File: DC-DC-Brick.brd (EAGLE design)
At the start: 48.5 x 76.2 mm, 20 parts

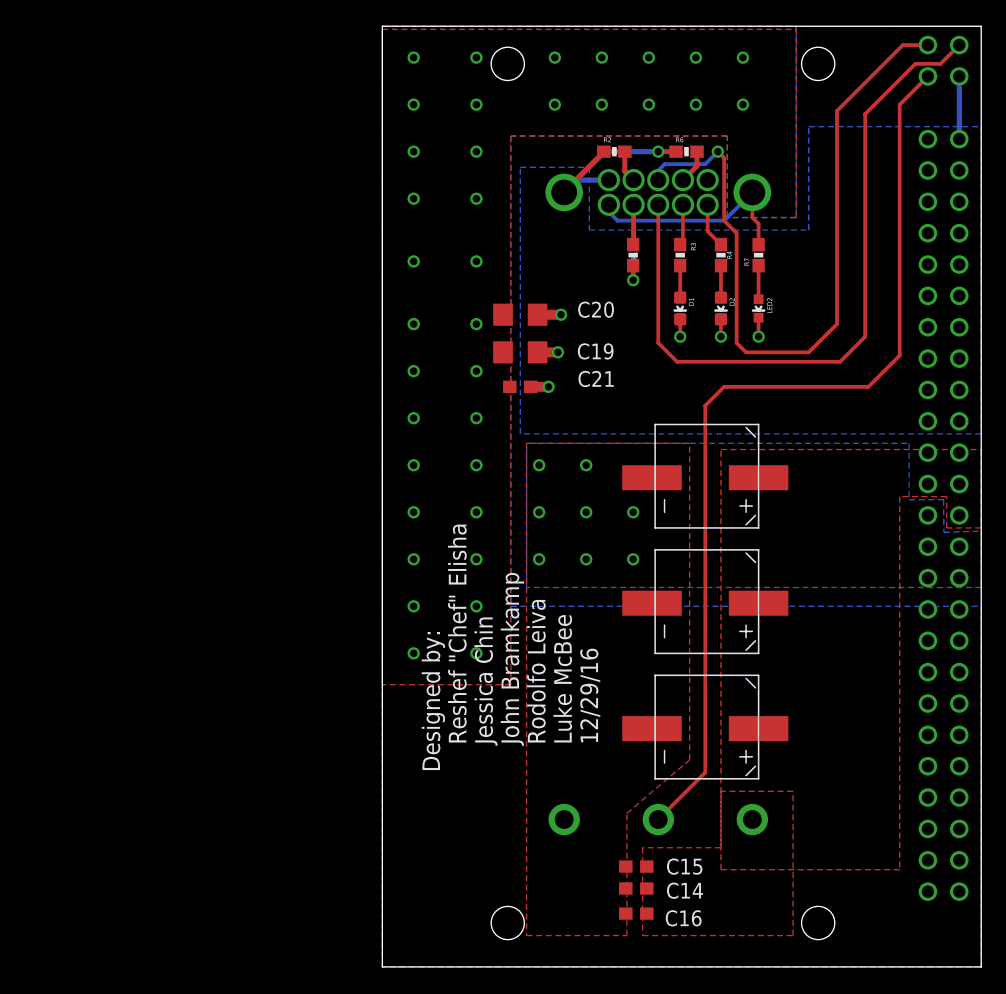
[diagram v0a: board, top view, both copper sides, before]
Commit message: Power brick connectors edited
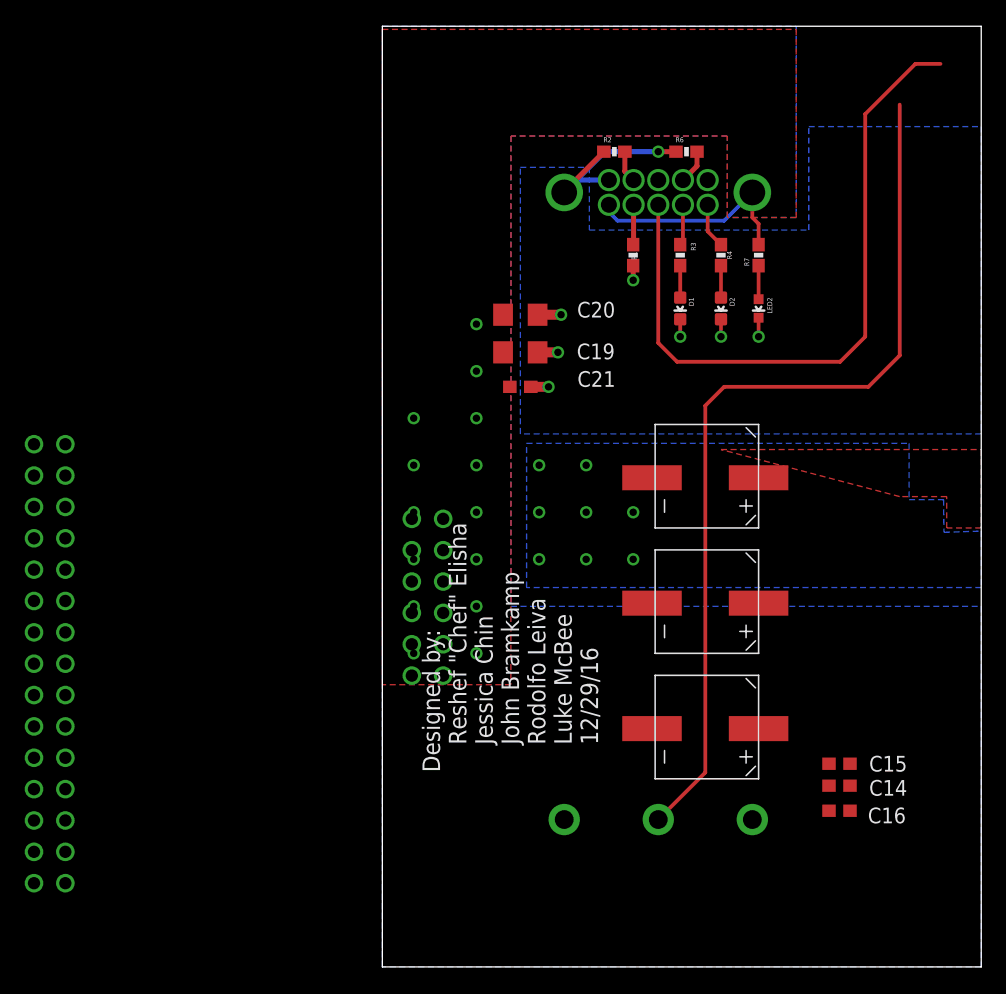
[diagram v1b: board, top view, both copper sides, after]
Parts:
- added U$2: POWER_BRICK_CONNECTORS(2X6), MotherBoardParts2:POWER_BRICK_CONNECTORS(2X6)
- U$3: value POWER-BRICK-CONNECTOR -> POWER_BRICK_CONNECTORS(2X15); device MotherboardParts:POWER-BRICK-CONNECTOR -> MotherBoardParts2:POWER_BRICK_CONNECTORS(2X15)
- moved U$3 74.4 mm to (-26.9, 23.3)
- moved C14 18.4 mm to (37.0, 14.7)
- moved C15 18.4 mm to (37.0, 16.5)
- moved C16 18.4 mm to (37.0, 12.6)
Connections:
- removed net N$10: U$1.10, U$3.P$54
- removed net N$8: U$1.11, U$3.P$53
- removed net V+: C19.1, C20.1, C21.1, R7.2, U$1.16, U$1.6, U$3.P$1, U$3.P$10, U$3.P$11, U$3.P$12, U$3.P$13, U$3.P$14, U$3.P$15, U$3.P$16, U$3.P$17, U$3.P$18, U$3.P$19, U$3.P$2, U$3.P$20, U$3.P$3, U$3.P$4, U$3.P$5, U$3.P$6, U$3.P$7, U$3.P$8, U$3.P$9
- removed net VCC: C14.1, C15.1, C16.1, C22V1.P$3, C22V5.P$3, C22V6.P$3, U$1.1, U$3.P$26, U$3.P$27, U$3.P$28, U$3.P$29, U$3.P$30
- new net +12V: C19.1, C20.1, C21.1, R7.2, U$1.16, U$1.6, U$3.P$1, U$3.P$16, U$3.P$17, U$3.P$18, U$3.P$19, U$3.P$2, U$3.P$20, U$3.P$21, U$3.P$22, U$3.P$3, U$3.P$4, U$3.P$5, U$3.P$6, U$3.P$7
- new net 48V: C14.1, C15.1, C16.1, C22V1.P$3, C22V5.P$3, C22V6.P$3, U$1.1, U$2.P$1, U$2.P$2, U$2.P$7, U$2.P$8
- new net 48V_GND: C14.2, C15.2, C16.2, C22V1.P$1, C22V5.P$1, C22V6.P$1, U$2.P$10, U$2.P$3, U$2.P$4, U$2.P$9
- new net SCL: U$1.10, U$2.P$12
- new net SDA: U$1.11, U$2.P$6
- net GND: now also U$2.P$5, U$3.P$10, U$3.P$11, U$3.P$12, U$3.P$13, U$3.P$14, U$3.P$15, U$3.P$24, U$3.P$25, U$3.P$26, U$3.P$27, U$3.P$28, U$3.P$29, U$3.P$30, U$3.P$9; no longer U$3.P$31, U$3.P$32, U$3.P$33, U$3.P$34, U$3.P$35, U$3.P$36, U$3.P$37, U$3.P$38, U$3.P$39, U$3.P$40, U$3.P$41, U$3.P$42, U$3.P$43, U$3.P$44, U$3.P$45, U$3.P$46, U$3.P$47, U$3.P$48, U$3.P$49, U$3.P$50, U$3.P$52
- net ON/OFF: now also U$2.P$11; no longer U$3.P$51
- net V-: no longer C14.2, C15.2, C16.2, C22V1.P$1, C22V5.P$1, C22V6.P$1, U$3.P$21, U$3.P$22, U$3.P$23, U$3.P$24, U$3.P$25
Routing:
- net N$8: track 58.6 -> 0.00 mm, vias 1 -> 0
- net N$10: track 57.4 -> 0.00 mm
- net SCL: track 0.00 -> 55.2 mm
- net V+: track 17.9 -> 0.00 mm, vias 36 -> 0
- net +12V: track 0.00 -> 17.9 mm, vias 0 -> 14
- net GND: track 34.7 -> 29.6 mm
- net ON/OFF: track 76.1 -> 72.9 mm
- added copper zone on layer 1, net +12V
- added copper zone on layer 16, net +12V
- added copper zone on layer 1, net 48V
- removed copper zone on layer 1, net V+
- removed copper zone on layer 16, net V+
- removed copper zone on layer 1, net V-
- removed copper zone on layer 1, net VCC

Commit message: New power brick board
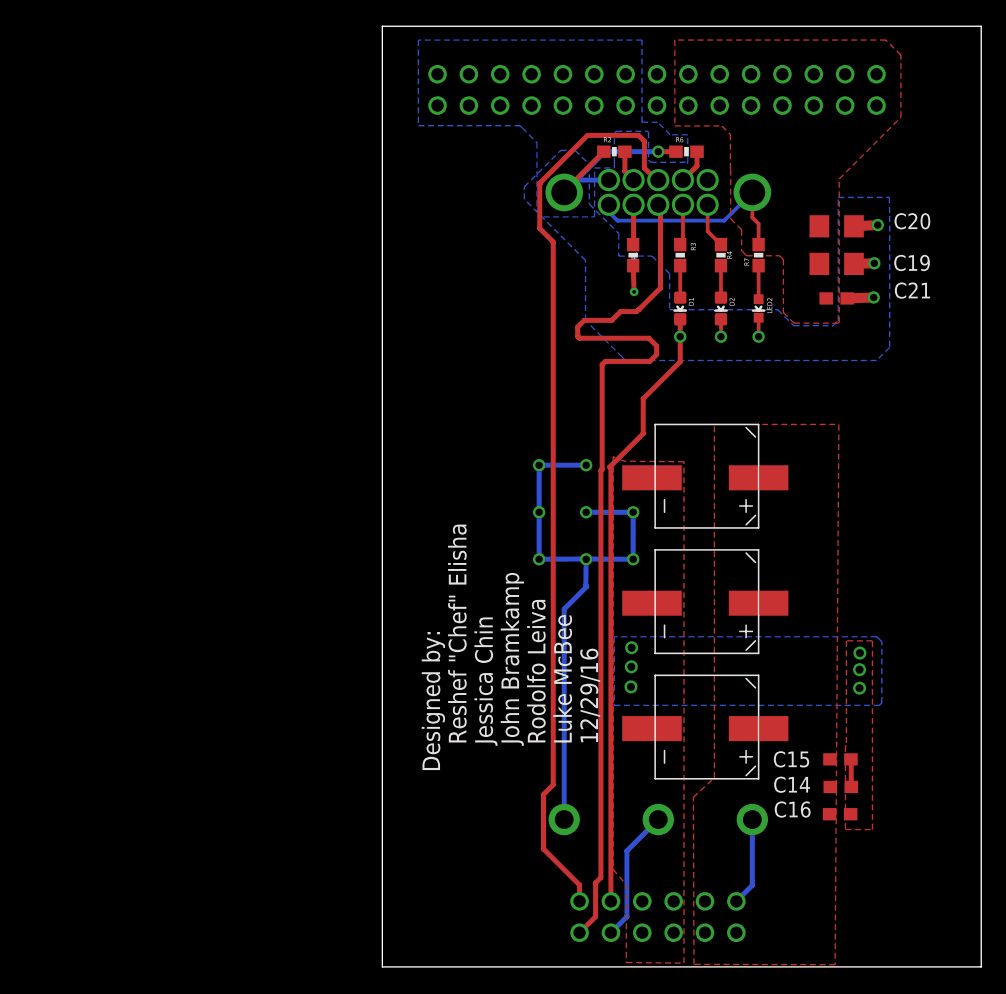
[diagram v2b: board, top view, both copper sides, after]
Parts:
- moved U$3 67.7 mm to (21.0, 71.0), turned to 270 degrees
- moved U$2 31.9 mm to (22.3, 4.04), turned to 270 degrees
- moved C19 26.6 mm to (36.8, 56.9)
- moved C20 26.6 mm to (36.8, 60.0)
- moved C21 26.6 mm to (36.8, 54.2)
- moved C15 0.36 mm to (37.1, 16.8), turned to 0 degrees
- moved C16 0.28 mm to (37.1, 12.4), turned to 0 degrees
- moved C14 0.14 mm to (37.1, 14.6), turned to 0 degrees
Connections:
- net +12V renamed 12V
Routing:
- net SDA: track 0.00 -> 74.1 mm
- net ON/OFF: track 72.9 -> 10.8 mm
- net GND: track 29.6 -> 79.5 mm
- net V-: track 0.00 -> 48.6 mm
- net SCL: track 55.2 -> 74.5 mm
- net 48V: track 0.00 -> 7.17 mm
- net 48V_GND: track 0.00 -> 2.25 mm, vias 0 -> 6
- net 12V: vias 14 -> 0
- added copper zone on layer 1, net 48V_GND
- added copper zone on layer 16, net 48V_GND
- removed copper zone on layer 16, net 12V
- removed copper zone on layer 16, net V-

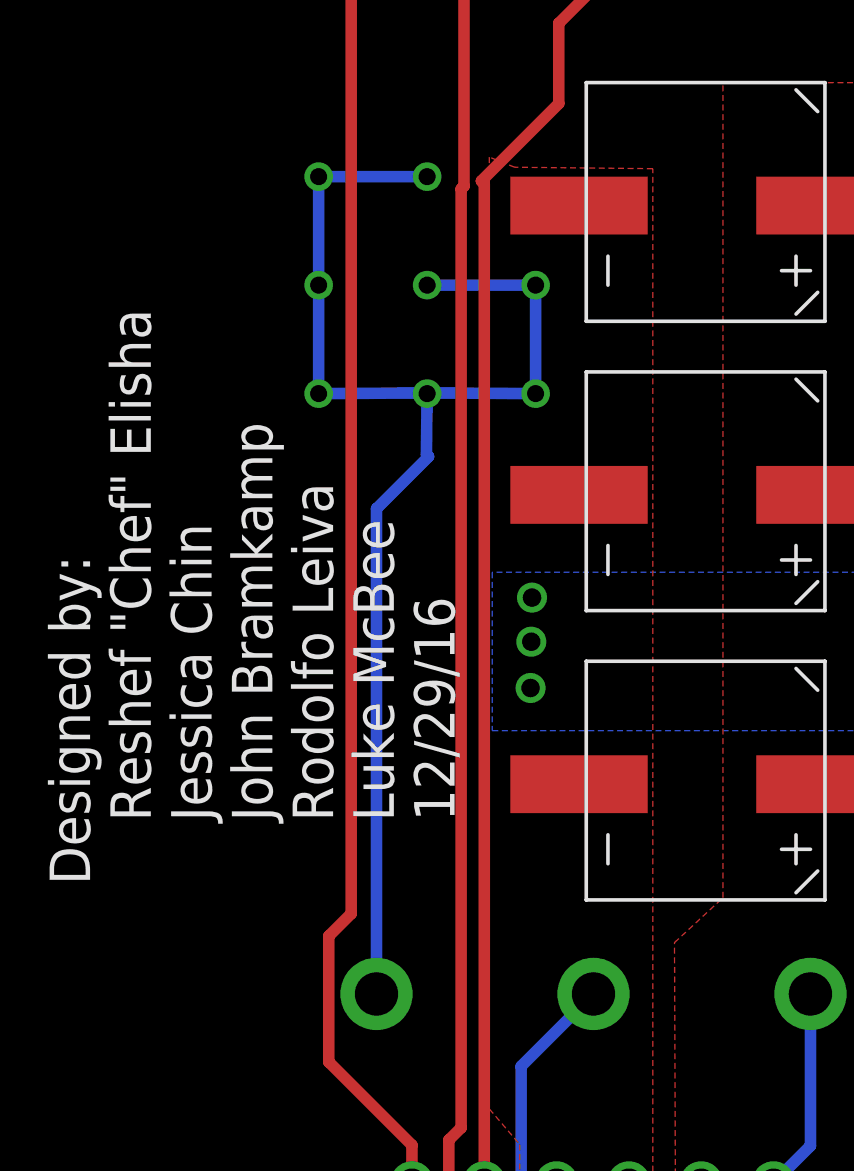
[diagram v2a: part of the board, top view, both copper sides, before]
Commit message: Edit Signal Name
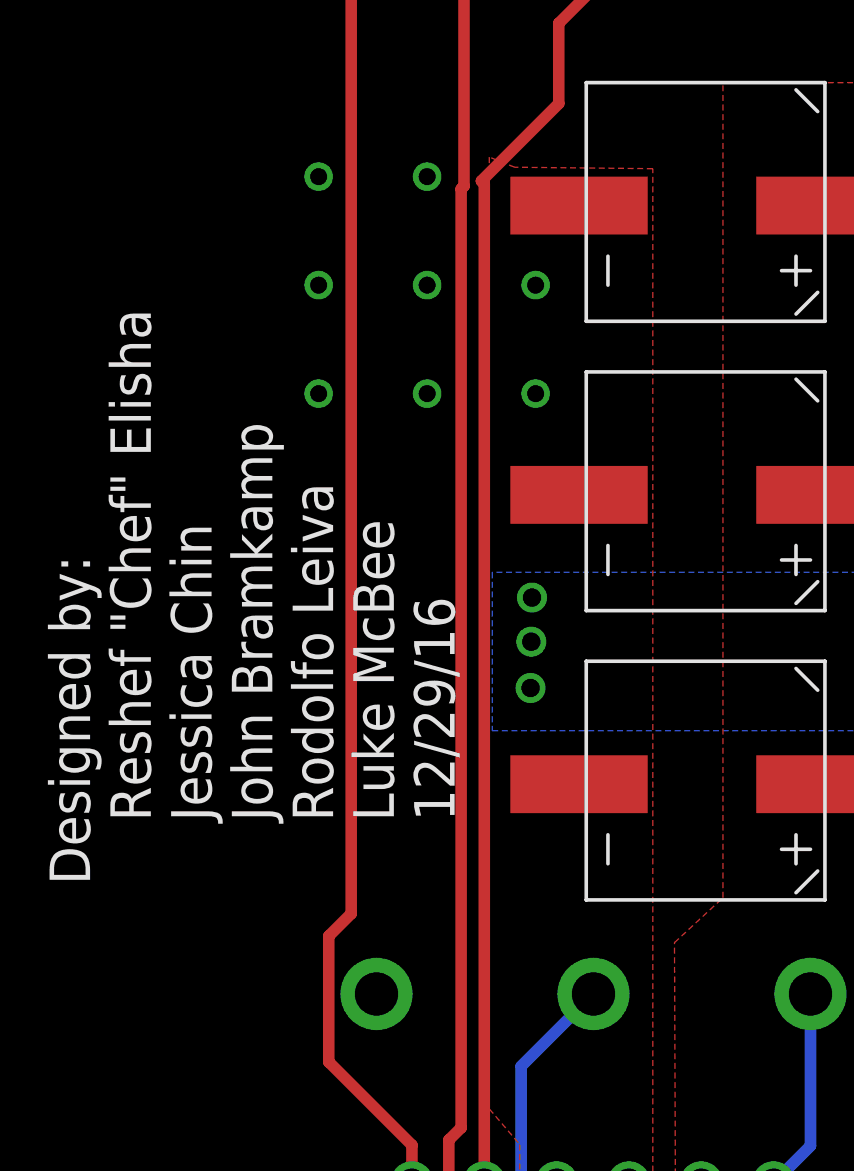
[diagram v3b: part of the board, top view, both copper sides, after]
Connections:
- removed net V-: U$1.4
- net 48V_GND: now also U$1.4
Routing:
- net V-: track 48.6 -> 0.00 mm, vias 8 -> 0
- net 48V_GND: track 2.25 -> 2.27 mm, vias 6 -> 14
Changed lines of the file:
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@@
 <?xml version="1.0" encoding="utf-8"?>
 <!DOCTYPE eagle SYSTEM "eagle.dtd">
-<eagle version="8.4.2">
+<eagle version="8.4.1">
 <drawing>
 <settings>
@@
 <wire x1="29.972" y1="6.604" x2="29.972" y2="11.938" width="0.4064" layer="16"/>
 </signal>
-<signal name="V-">
-<contactref element="U$1" pad="4"/>
-<via x="12.7" y="40.64" extent="1-16" drill="0.6"/>
-<via x="16.51" y="40.64" extent="1-16" drill="0.6"/>
-<via x="16.51" y="36.83" extent="1-16" drill="0.6"/>
-<via x="12.7" y="36.83" extent="1-16" drill="0.6"/>
-<via x="12.7" y="33.02" extent="1-16" drill="0.6"/>
-<via x="16.51" y="33.02" extent="1-16" drill="0.6"/>
-<via x="20.32" y="33.02" extent="1-16" drill="0.6"/>
-<via x="20.32" y="36.83" extent="1-16" drill="0.6"/>
-<wire x1="14.732" y1="11.938" x2="14.732" y2="28.9814" width="0.4064" layer="16"/>
-<wire x1="14.732" y1="28.9814" x2="16.5608" y2="30.8102" width="0.4064" layer="16"/>
-<wire x1="20.32" y1="33.02" x2="20.32" y2="36.83" width="0.4064" layer="16"/>
-<wire x1="12.7" y1="36.83" x2="12.7" y2="33.02" width="0.4064" layer="16"/>
-<wire x1="12.7" y1="36.83" x2="12.7" y2="40.64" width="0.4064" layer="16"/>
-<wire x1="12.7" y1="40.64" x2="16.51" y2="40.64" width="0.4064" layer="16"/>
-<wire x1="16.51" y1="33.0454" x2="20.32" y2="33.02" width="0.4064" layer="16"/>
-<wire x1="20.32" y1="36.83" x2="16.51" y2="36.83" width="0.4064" layer="16"/>
-<wire x1="16.5608" y1="30.8102" x2="16.4846" y2="30.8864" width="0.4064" layer="16"/>
-<wire x1="16.4846" y1="30.8864" x2="16.51" y2="33.0454" width="0.4064" layer="16"/>
-<wire x1="12.7" y1="33.02" x2="16.51" y2="33.0454" width="0.4064" layer="16"/>
-<wire x1="16.51" y1="33.02" x2="16.51" y2="33.0454" width="0.4064" layer="16"/>
-</signal>
 <signal name="N$12">
 <contactref element="LED2" pad="A"/>
@@
 <wire x1="37.9594" y1="16.8148" x2="37.9848" y2="16.7894" width="0.4064" layer="1"/>
 <wire x1="37.9848" y1="16.7894" x2="37.9848" y2="14.5796" width="0.4064" layer="1"/>
+<contactref element="U$1" pad="4"/>
+<via x="12.7" y="40.64" extent="1-16" drill="0.6"/>
+<via x="16.51" y="40.64" extent="1-16" drill="0.6"/>
+<via x="16.51" y="36.83" extent="1-16" drill="0.6"/>
+<via x="12.7" y="36.83" extent="1-16" drill="0.6"/>
+<via x="12.7" y="33.02" extent="1-16" drill="0.6"/>
+<via x="16.51" y="33.02" extent="1-16" drill="0.6"/>
+<via x="20.32" y="33.02" extent="1-16" drill="0.6"/>
+<via x="20.32" y="36.83" extent="1-16" drill="0.6"/>
+<wire x1="16.51" y1="33.02" x2="16.51" y2="33.0454" width="0.4064" layer="16"/>
+<wire x1="12.7" y1="40.64" x2="16.51" y2="40.64" width="0" layer="19" extent="1-1"/>
+<wire x1="16.51" y1="36.83" x2="16.51" y2="40.64" width="0" layer="19" extent="1-1"/>
+<wire x1="16.51" y1="33.0454" x2="16.51" y2="36.83" width="0" layer="19" extent="16-16"/>
+<wire x1="12.7" y1="36.83" x2="12.7" y2="40.64" width="0" layer="19" extent="1-1"/>
+<wire x1="12.7" y1="33.02" x2="16.51" y2="33.02" width="0" layer="19" extent="1-1"/>
+<wire x1="20.32" y1="36.83" x2="16.51" y2="36.83" width="0" layer="19" extent="1-1"/>
+<wire x1="14.732" y1="11.938" x2="21.0566" y2="5.3086" width="0" layer="19" extent="1-1"/>
 </signal>
 </signals>

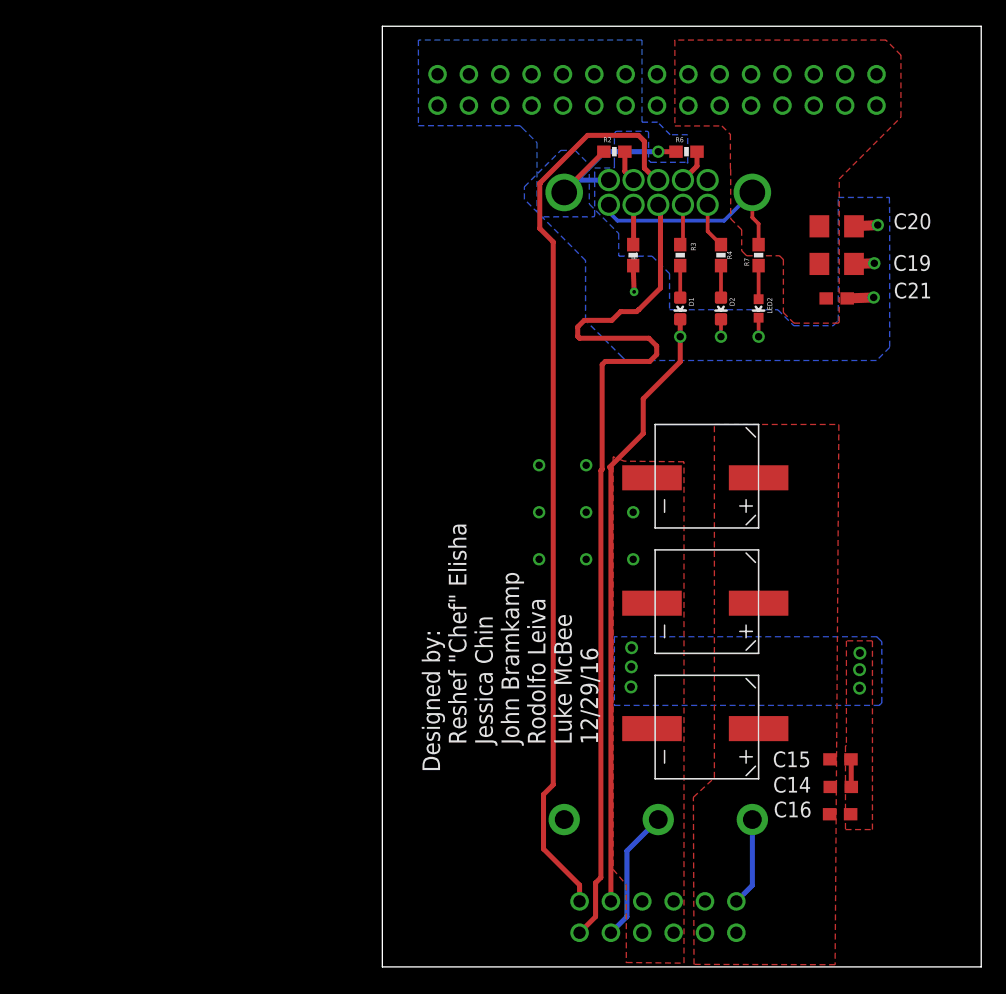
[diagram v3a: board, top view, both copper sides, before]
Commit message: fixed 48V_return on layout
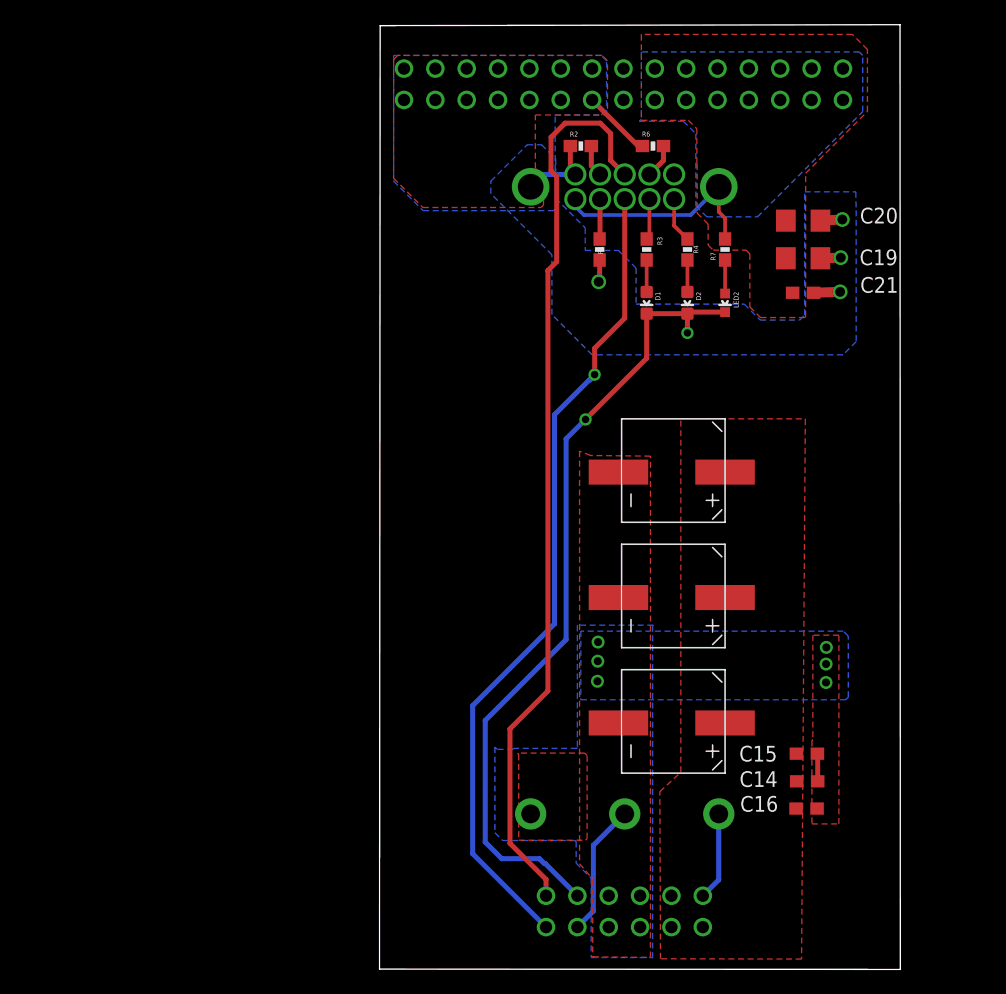
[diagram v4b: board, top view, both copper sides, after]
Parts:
- moved C16 2.76 mm to (34.4, 12.8)
- moved C19 2.76 mm to (34.1, 57.4)
- moved C20 2.76 mm to (34.1, 60.5)
- moved C21 2.76 mm to (34.1, 54.6)
- moved C15 2.76 mm to (34.4, 17.3)
- moved C22V1 2.76 mm to (19.4, 44.4)
- moved C22V5 2.76 mm to (19.4, 34.2)
- moved C22V6 2.76 mm to (19.4, 24.1)
- moved R1 2.76 mm to (17.6, 58.1)
- moved R2 2.76 mm to (16.1, 66.5)
- moved R3 2.76 mm to (21.4, 58.1)
- moved R6 2.76 mm to (21.9, 66.5)
- moved R7 2.76 mm to (27.8, 58.1)
- moved U$1 2.76 mm to (19.6, 37.8)
- moved U$2 2.76 mm to (19.6, 4.50)
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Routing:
- net SCL: track 74.5 -> 66.6 mm, vias 0 -> 1
- net GND: track 79.5 -> 85.8 mm, vias 8 -> 6
- net 48V_GND: track 2.27 -> 2.25 mm, vias 14 -> 6
- added copper zone on layer 16, net 12V
- added copper zone on layer 1, net GND
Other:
- board size 48.5 x 76.2 mm -> 42.2 x 76.5 mm
- board text removed: "Designed by: Reshef "Chef" Elisha Jessica Chin John Bramkamp Rodolfo Leiva Luke McBee 12/29/16"
